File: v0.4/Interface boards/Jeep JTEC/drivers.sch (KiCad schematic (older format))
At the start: 10 parts

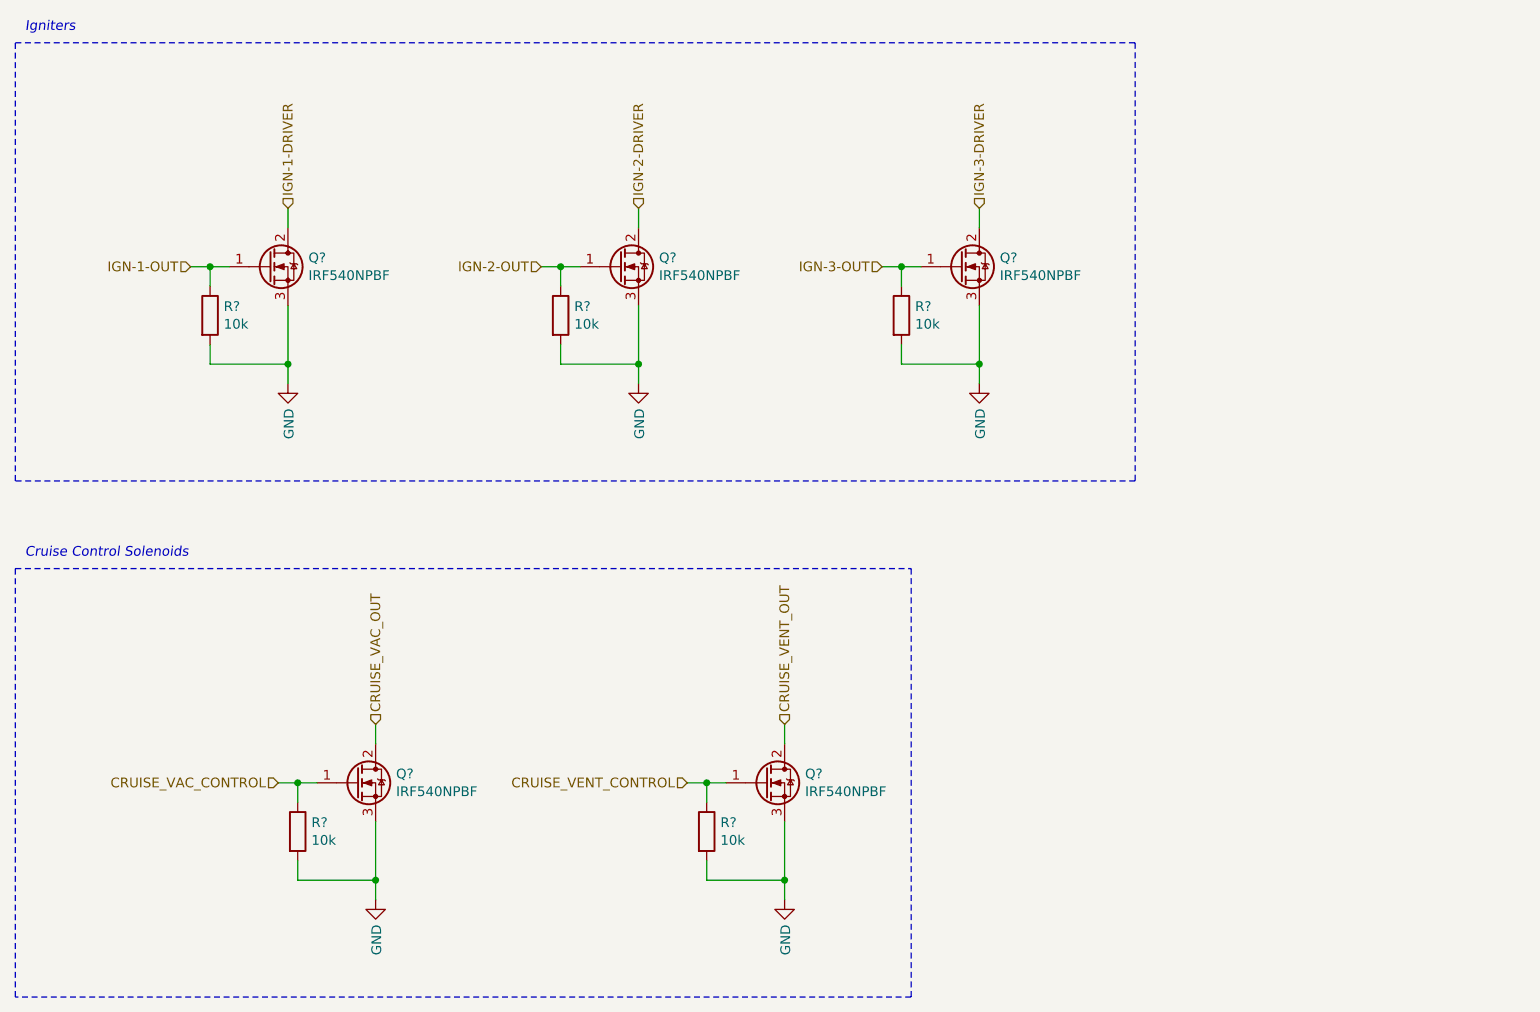
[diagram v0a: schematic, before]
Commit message: Add voltage sense circuit for alternator control
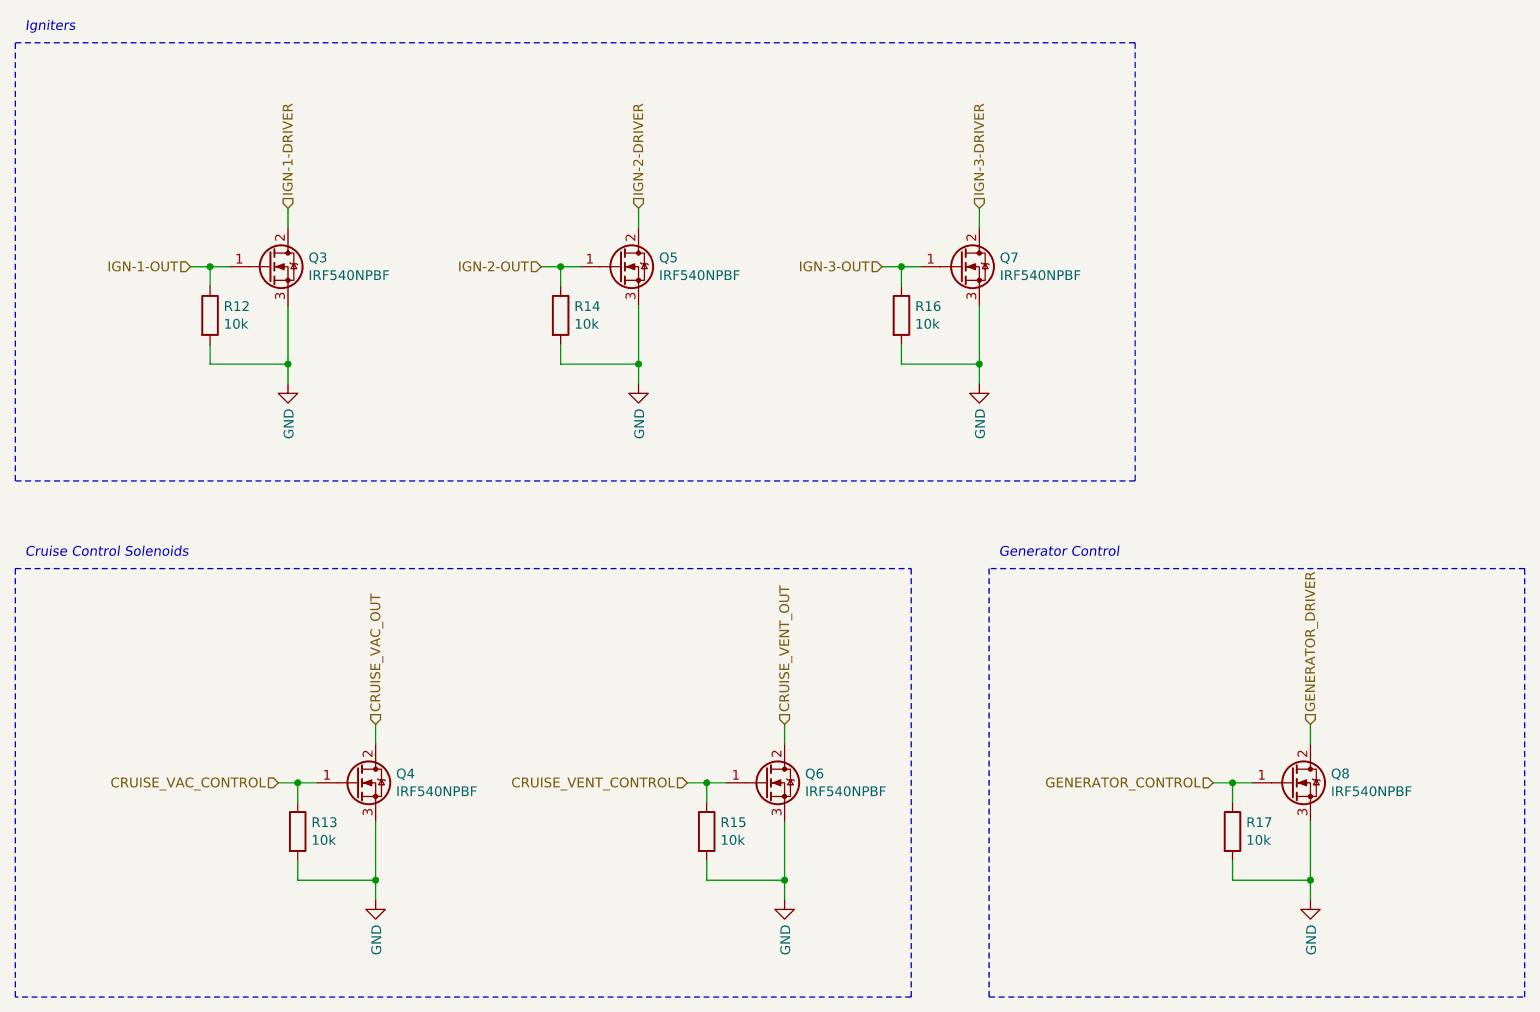
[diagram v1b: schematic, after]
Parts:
- added Q8: IRF540NPBF, Package_TO_SOT_THT:TO-220-3_Vertical, symbol Transistor_FET:IRF540N
- added R17: 10k, Resistor_SMD:R_0805_2012Metric, symbol Device:R
- R12, R13, R14, R15, R16: renamed from R?; footprint (none) -> Resistor_SMD:R_0805_2012Metric
- gave numbers to parts that had none: 5
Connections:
- net GND: now also Q8.3 (S), R17.2
- new net GENERATOR_CONTROL: Q8.1 (G), R17.1
- new net GENERATOR_DRIVER: Q8.2 (D)
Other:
- note added: "Generator Control"
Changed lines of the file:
@@
 P 2200 2050
 AR Path="/616A5EE0" Ref="Q?"  Part="1"
-AR Path="/6169594B/616A5EE0" Ref="Q?"  Part="1"
-F 0 "Q?" H 2405 2096 50  0000 L CNN
+AR Path="/6169594B/616A5EE0" Ref="Q3"  Part="1"
+F 0 "Q3" H 2405 2096 50  0000 L CNN
 F 1 "IRF540NPBF" H 2405 2005 50  0000 L CNN
 F 2 "Package_TO_SOT_THT:TO-220-3_Vertical" H 2450 1975 50  0001 L CIN
@@
 P 2300 2650
 AR Path="/616A5EE6" Ref="#PWR?"  Part="1"
-AR Path="/6169594B/616A5EE6" Ref="#PWR?"  Part="1"
-F 0 "#PWR?" H 2300 2400 50  0001 C CNN
+AR Path="/6169594B/616A5EE6" Ref="#PWR027"  Part="1"
+F 0 "#PWR027" H 2300 2400 50  0001 C CNN
 F 1 "GND" V 2305 2522 50  0000 R CNN
 F 2 "" H 2300 2650 50  0001 C CNN
@@
 AR Path="/615FCF77/616A5EF0" Ref="R?"  Part="1"
 AR Path="/616A5EF0" Ref="R?"  Part="1"
-AR Path="/6169594B/616A5EF0" Ref="R?"  Part="1"
-F 0 "R?" H 1970 2346 50  0000 L CNN
+AR Path="/6169594B/616A5EF0" Ref="R12"  Part="1"
+F 0 "R12" H 1970 2346 50  0000 L CNN
 F 1 "10k" H 1970 2255 50  0000 L CNN
-F 2 "" V 1830 2300 50  0001 C CNN
+F 2 "Resistor_SMD:R_0805_2012Metric" V 1830 2300 50  0001 C CNN
 F 3 "~" H 1900 2300 50  0001 C CNN
 	1    1900 2300
@@
 P 4000 2050
 AR Path="/616A5EFE" Ref="Q?"  Part="1"
-AR Path="/6169594B/616A5EFE" Ref="Q?"  Part="1"
-F 0 "Q?" H 4205 2096 50  0000 L CNN
+AR Path="/6169594B/616A5EFE" Ref="Q5"  Part="1"
+F 0 "Q5" H 4205 2096 50  0000 L CNN
 F 1 "IRF540NPBF" H 4205 2005 50  0000 L CNN
 F 2 "Package_TO_SOT_THT:TO-220-3_Vertical" H 4250 1975 50  0001 L CIN
@@
 P 4100 2650
 AR Path="/616A5F04" Ref="#PWR?"  Part="1"
-AR Path="/6169594B/616A5F04" Ref="#PWR?"  Part="1"
-F 0 "#PWR?" H 4100 2400 50  0001 C CNN
+AR Path="/6169594B/616A5F04" Ref="#PWR029"  Part="1"
+F 0 "#PWR029" H 4100 2400 50  0001 C CNN
 F 1 "GND" V 4105 2522 50  0000 R CNN
 F 2 "" H 4100 2650 50  0001 C CNN
@@
 AR Path="/615FCF77/616A5F0E" Ref="R?"  Part="1"
 AR Path="/616A5F0E" Ref="R?"  Part="1"
-AR Path="/6169594B/616A5F0E" Ref="R?"  Part="1"
-F 0 "R?" H 3770 2346 50  0000 L CNN
+AR Path="/6169594B/616A5F0E" Ref="R14"  Part="1"
+F 0 "R14" H 3770 2346 50  0000 L CNN
 F 1 "10k" H 3770 2255 50  0000 L CNN
-F 2 "" V 3630 2300 50  0001 C CNN
+F 2 "Resistor_SMD:R_0805_2012Metric" V 3630 2300 50  0001 C CNN
 F 3 "~" H 3700 2300 50  0001 C CNN
 	1    3700 2300
@@
 P 5750 2050
 AR Path="/616A8D7B" Ref="Q?"  Part="1"
-AR Path="/6169594B/616A8D7B" Ref="Q?"  Part="1"
-F 0 "Q?" H 5955 2096 50  0000 L CNN
+AR Path="/6169594B/616A8D7B" Ref="Q7"  Part="1"
+F 0 "Q7" H 5955 2096 50  0000 L CNN
 F 1 "IRF540NPBF" H 5955 2005 50  0000 L CNN
 F 2 "Package_TO_SOT_THT:TO-220-3_Vertical" H 6000 1975 50  0001 L CIN
@@
 P 5850 2650
 AR Path="/616A8D81" Ref="#PWR?"  Part="1"
-AR Path="/6169594B/616A8D81" Ref="#PWR?"  Part="1"
-F 0 "#PWR?" H 5850 2400 50  0001 C CNN
+AR Path="/6169594B/616A8D81" Ref="#PWR031"  Part="1"
+F 0 "#PWR031" H 5850 2400 50  0001 C CNN
 F 1 "GND" V 5855 2522 50  0000 R CNN
 F 2 "" H 5850 2650 50  0001 C CNN
@@
 AR Path="/615FCF77/616A8D8B" Ref="R?"  Part="1"
 AR Path="/616A8D8B" Ref="R?"  Part="1"
-AR Path="/6169594B/616A8D8B" Ref="R?"  Part="1"
-F 0 "R?" H 5520 2346 50  0000 L CNN
+AR Path="/6169594B/616A8D8B" Ref="R16"  Part="1"
+F 0 "R16" H 5520 2346 50  0000 L CNN
 F 1 "10k" H 5520 2255 50  0000 L CNN
-F 2 "" V 5380 2300 50  0001 C CNN
+F 2 "Resistor_SMD:R_0805_2012Metric" V 5380 2300 50  0001 C CNN
 F 3 "~" H 5450 2300 50  0001 C CNN
 	1    5450 2300
@@
 P 2650 4700
 AR Path="/61801B89" Ref="Q?"  Part="1"
-AR Path="/6169594B/61801B89" Ref="Q?"  Part="1"
-F 0 "Q?" H 2855 4746 50  0000 L CNN
+AR Path="/6169594B/61801B89" Ref="Q4"  Part="1"
+F 0 "Q4" H 2855 4746 50  0000 L CNN
 F 1 "IRF540NPBF" H 2855 4655 50  0000 L CNN
 F 2 "Package_TO_SOT_THT:TO-220-3_Vertical" H 2900 4625 50  0001 L CIN
@@
 P 2750 5300
 AR Path="/61801B8F" Ref="#PWR?"  Part="1"
-AR Path="/6169594B/61801B8F" Ref="#PWR?"  Part="1"
-F 0 "#PWR?" H 2750 5050 50  0001 C CNN
+AR Path="/6169594B/61801B8F" Ref="#PWR028"  Part="1"
+F 0 "#PWR028" H 2750 5050 50  0001 C CNN
 F 1 "GND" V 2755 5172 50  0000 R CNN
 F 2 "" H 2750 5300 50  0001 C CNN
@@
 AR Path="/615FCF77/61801B95" Ref="R?"  Part="1"
 AR Path="/61801B95" Ref="R?"  Part="1"
-AR Path="/6169594B/61801B95" Ref="R?"  Part="1"
-F 0 "R?" H 2420 4996 50  0000 L CNN
+AR Path="/6169594B/61801B95" Ref="R13"  Part="1"
+F 0 "R13" H 2420 4996 50  0000 L CNN
 F 1 "10k" H 2420 4905 50  0000 L CNN
-F 2 "" V 2280 4950 50  0001 C CNN
+F 2 "Resistor_SMD:R_0805_2012Metric" V 2280 4950 50  0001 C CNN
 F 3 "~" H 2350 4950 50  0001 C CNN
 	1    2350 4950
@@
 P 4750 4700
 AR Path="/61801B9B" Ref="Q?"  Part="1"
-AR Path="/6169594B/61801B9B" Ref="Q?"  Part="1"
-F 0 "Q?" H 4955 4746 50  0000 L CNN
+AR Path="/6169594B/61801B9B" Ref="Q6"  Part="1"
+F 0 "Q6" H 4955 4746 50  0000 L CNN
 F 1 "IRF540NPBF" H 4955 4655 50  0000 L CNN
 F 2 "Package_TO_SOT_THT:TO-220-3_Vertical" H 5000 4625 50  0001 L CIN
@@
 P 4850 5300
 AR Path="/61801BA1" Ref="#PWR?"  Part="1"
-AR Path="/6169594B/61801BA1" Ref="#PWR?"  Part="1"
-F 0 "#PWR?" H 4850 5050 50  0001 C CNN
+AR Path="/6169594B/61801BA1" Ref="#PWR030"  Part="1"
+F 0 "#PWR030" H 4850 5050 50  0001 C CNN
 F 1 "GND" V 4855 5172 50  0000 R CNN
 F 2 "" H 4850 5300 50  0001 C CNN
@@
 AR Path="/615FCF77/61801BA7" Ref="R?"  Part="1"
 AR Path="/61801BA7" Ref="R?"  Part="1"
-AR Path="/6169594B/61801BA7" Ref="R?"  Part="1"
-F 0 "R?" H 4520 4996 50  0000 L CNN
+AR Path="/6169594B/61801BA7" Ref="R15"  Part="1"
+F 0 "R15" H 4520 4996 50  0000 L CNN
 F 1 "10k" H 4520 4905 50  0000 L CNN
-F 2 "" V 4380 4950 50  0001 C CNN
+F 2 "Resistor_SMD:R_0805_2012Metric" V 4380 4950 50  0001 C CNN
 F 3 "~" H 4450 4950 50  0001 C CNN
 	1    4450 4950
@@
 Text HLabel 4850 4400 1    50   Input ~ 0
 CRUISE_VENT_OUT
+Wire Wire Line
+	7050 4700 7150 4700
+Wire Wire Line
+	7550 4500 7550 4400
+Wire Wire Line
+	7150 4800 7150 4700
+Connection ~ 7150 4700
+Wire Wire Line
+	7150 4700 7250 4700
+Wire Wire Line
+	7150 5100 7150 5200
+Wire Wire Line
+	7150 5200 7550 5200
+Wire Wire Line
+	7550 5200 7550 5300
+Wire Wire Line
+	7550 4900 7550 5200
+Connection ~ 7550 5200
+$Comp
+L Transistor_FET:IRF540N Q?
+U 1 1 61888343
+P 7450 4700
+AR Path="/61888343" Ref="Q?"  Part="1"
+AR Path="/6169594B/61888343" Ref="Q8"  Part="1"
+F 0 "Q8" H 7655 4746 50  0000 L CNN
+F 1 "IRF540NPBF" H 7655 4655 50  0000 L CNN
+F 2 "Package_TO_SOT_THT:TO-220-3_Vertical" H 7700 4625 50  0001 L CIN
+F 3 "http://www.irf.com/product-info/datasheets/data/irf540n.pdf" H 7450 4700 50  0001 L CNN
+	1    7450 4700
+	1    0    0    -1
+$EndComp
+$Comp
+L power:GND #PWR?
+U 1 1 61888349
+P 7550 5300
+AR Path="/61888349" Ref="#PWR?"  Part="1"
+AR Path="/6169594B/61888349" Ref="#PWR032"  Part="1"
+F 0 "#PWR032" H 7550 5050 50  0001 C CNN
+F 1 "GND" V 7555 5172 50  0000 R CNN
+F 2 "" H 7550 5300 50  0001 C CNN
+F 3 "" H 7550 5300 50  0001 C CNN
+	1    7550 5300
+	1    0    0    -1
+$EndComp
+$Comp
+L Device:R R?
+U 1 1 6188834F
+P 7150 4950
+AR Path="/615FCF77/6188834F" Ref="R?"  Part="1"
+AR Path="/6188834F" Ref="R?"  Part="1"
+AR Path="/6169594B/6188834F" Ref="R17"  Part="1"
+F 0 "R17" H 7220 4996 50  0000 L CNN
+F 1 "10k" H 7220 4905 50  0000 L CNN
+F 2 "Resistor_SMD:R_0805_2012Metric" V 7080 4950 50  0001 C CNN
+F 3 "~" H 7150 4950 50  0001 C CNN
+	1    7150 4950
+	1    0    0    -1
+$EndComp
+Text HLabel 7050 4700 0    50   Input ~ 0
+GENERATOR_CONTROL
+Text HLabel 7550 4400 1    50   Input ~ 0
+GENERATOR_DRIVER
+Wire Notes Line
+	5900 3600 5900 5800
+Wire Notes Line
+	5900 5800 8650 5800
+Wire Notes Line
+	8650 5800 8650 3600
+Wire Notes Line
+	8650 3600 5900 3600
+Text Notes 5950 3550 0    50   Italic 0
+Generator Control
 $EndSCHEMATC

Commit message: Add BOM items for jellybean parts
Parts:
- Q3, Q4, Q5, Q6, Q7, Q8: Manufacturer (none) -> Infineon; Manufacturer# (none) -> IRF540NPBF
- R12, R13, R14, R15, R16, R17: Manufacturer (none) -> Yageo; Manufacturer# (none) -> RC0805FR-0710KL
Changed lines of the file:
@@
 EESchema Schematic File Version 4
+LIBS:Jeep JTEC-cache
 EELAYER 30 0
 EELAYER END
@@
 F 2 "Package_TO_SOT_THT:TO-220-3_Vertical" H 2450 1975 50  0001 L CIN
 F 3 "http://www.irf.com/product-info/datasheets/data/irf540n.pdf" H 2200 2050 50  0001 L CNN
+F 4 "Infineon" H 2200 2050 50  0001 C CNN "Manufacturer"
+F 5 "IRF540NPBF" H 2200 2050 50  0001 C CNN "Manufacturer#"
 	1    2200 2050
 	1    0    0    -1
@@
 F 2 "Resistor_SMD:R_0805_2012Metric" V 1830 2300 50  0001 C CNN
 F 3 "~" H 1900 2300 50  0001 C CNN
+F 4 "Yageo" H 1900 2300 50  0001 C CNN "Manufacturer"
+F 5 "RC0805FR-0710KL" H 1900 2300 50  0001 C CNN "Manufacturer#"
 	1    1900 2300
 	1    0    0    -1
@@
 F 2 "Package_TO_SOT_THT:TO-220-3_Vertical" H 4250 1975 50  0001 L CIN
 F 3 "http://www.irf.com/product-info/datasheets/data/irf540n.pdf" H 4000 2050 50  0001 L CNN
+F 4 "Infineon" H 4000 2050 50  0001 C CNN "Manufacturer"
+F 5 "IRF540NPBF" H 4000 2050 50  0001 C CNN "Manufacturer#"
 	1    4000 2050
 	1    0    0    -1
@@
 F 2 "Resistor_SMD:R_0805_2012Metric" V 3630 2300 50  0001 C CNN
 F 3 "~" H 3700 2300 50  0001 C CNN
+F 4 "Yageo" H 3700 2300 50  0001 C CNN "Manufacturer"
+F 5 "RC0805FR-0710KL" H 3700 2300 50  0001 C CNN "Manufacturer#"
 	1    3700 2300
 	1    0    0    -1
@@
 F 2 "Package_TO_SOT_THT:TO-220-3_Vertical" H 6000 1975 50  0001 L CIN
 F 3 "http://www.irf.com/product-info/datasheets/data/irf540n.pdf" H 5750 2050 50  0001 L CNN
+F 4 "Infineon" H 5750 2050 50  0001 C CNN "Manufacturer"
+F 5 "IRF540NPBF" H 5750 2050 50  0001 C CNN "Manufacturer#"
 	1    5750 2050
 	1    0    0    -1
@@
 F 2 "Resistor_SMD:R_0805_2012Metric" V 5380 2300 50  0001 C CNN
 F 3 "~" H 5450 2300 50  0001 C CNN
+F 4 "Yageo" H 5450 2300 50  0001 C CNN "Manufacturer"
+F 5 "RC0805FR-0710KL" H 5450 2300 50  0001 C CNN "Manufacturer#"
 	1    5450 2300
 	1    0    0    -1
@@
 F 2 "Package_TO_SOT_THT:TO-220-3_Vertical" H 2900 4625 50  0001 L CIN
 F 3 "http://www.irf.com/product-info/datasheets/data/irf540n.pdf" H 2650 4700 50  0001 L CNN
+F 4 "Infineon" H 2650 4700 50  0001 C CNN "Manufacturer"
+F 5 "IRF540NPBF" H 2650 4700 50  0001 C CNN "Manufacturer#"
 	1    2650 4700
 	1    0    0    -1
@@
 F 2 "Resistor_SMD:R_0805_2012Metric" V 2280 4950 50  0001 C CNN
 F 3 "~" H 2350 4950 50  0001 C CNN
+F 4 "Yageo" H 2350 4950 50  0001 C CNN "Manufacturer"
+F 5 "RC0805FR-0710KL" H 2350 4950 50  0001 C CNN "Manufacturer#"
 	1    2350 4950
 	1    0    0    -1
@@
 F 2 "Package_TO_SOT_THT:TO-220-3_Vertical" H 5000 4625 50  0001 L CIN
 F 3 "http://www.irf.com/product-info/datasheets/data/irf540n.pdf" H 4750 4700 50  0001 L CNN
+F 4 "Infineon" H 4750 4700 50  0001 C CNN "Manufacturer"
+F 5 "IRF540NPBF" H 4750 4700 50  0001 C CNN "Manufacturer#"
 	1    4750 4700
 	1    0    0    -1
@@
 F 2 "Resistor_SMD:R_0805_2012Metric" V 4380 4950 50  0001 C CNN
 F 3 "~" H 4450 4950 50  0001 C CNN
+F 4 "Yageo" H 4450 4950 50  0001 C CNN "Manufacturer"
+F 5 "RC0805FR-0710KL" H 4450 4950 50  0001 C CNN "Manufacturer#"
 	1    4450 4950
 	1    0    0    -1
@@
 F 2 "Package_TO_SOT_THT:TO-220-3_Vertical" H 7700 4625 50  0001 L CIN
 F 3 "http://www.irf.com/product-info/datasheets/data/irf540n.pdf" H 7450 4700 50  0001 L CNN
+F 4 "Infineon" H 7450 4700 50  0001 C CNN "Manufacturer"
+F 5 "IRF540NPBF" H 7450 4700 50  0001 C CNN "Manufacturer#"
 	1    7450 4700
 	1    0    0    -1
@@
 F 2 "Resistor_SMD:R_0805_2012Metric" V 7080 4950 50  0001 C CNN
 F 3 "~" H 7150 4950 50  0001 C CNN
+F 4 "Yageo" H 7150 4950 50  0001 C CNN "Manufacturer"
+F 5 "RC0805FR-0710KL" H 7150 4950 50  0001 C CNN "Manufacturer#"
 	1    7150 4950
 	1    0    0    -1
